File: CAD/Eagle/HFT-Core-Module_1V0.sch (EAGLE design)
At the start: 372 parts, among them Q0521 ABS07-32.768KHZ, Q0811 ABM03B-32.000MHZ, Q0911 ABM3B-16MHZ-10-R50-1-U, T1201 MMBT2222, T1202 MMBT2222, T1203 MMBT2222, U0111 STM32L4Z_144PIN_SMPS, U0431 PAM2305AAB120, U0601 LM4120IM5-3.0, U0611 MAX5217, U0631 CFPT-141-20MHZ, U0641 OPA354, U0701 Si5338, U0801 SX1276, U0901 AX5243, U1011 MAX5136AGTG+, U1101 MCP3911A0-E-SS, U1121 OPA354, U1131 OPA354, U1141 OPA354, U1201 NHD-C0220BIZ_2X20CHARS, U1301 MPU-9250, U1311 MS5607-02BA03, U1321 SHT31-DIS, U1401 SOLARPANEL_3V3_5MA1_25MM_X_20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, U1402 SPV1040T, U1501 TS5A23166, U1601 PAM2305AAB330, U1701 TS5A23166, U1801 TS5A23166, U1901 TS5A23166, X1261 TTE_EN11-HSM, X2101 SMA_SMT_AMPHENOL-901-143, X2111 SMA_SMT_AMPHENOL-901-143, X2201 CUI SJ1-3535NS, X2211 CUI SJ1-3535NS, X2311 2X20/90_1MM27_HARWIN_M50-3202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, X2312 2X20/90_1MM27_HARWIN_M50-3202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, X2321 2X20/90_1MM27_HARWIN_M50-3202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, X2322 2X20/90_1MM27_HARWIN_M50-3202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, X2331 2X20/90_1MM27_HARWIN_M50-3202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, X2332 2X20/90_1MM27_HARWIN_M50-3202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

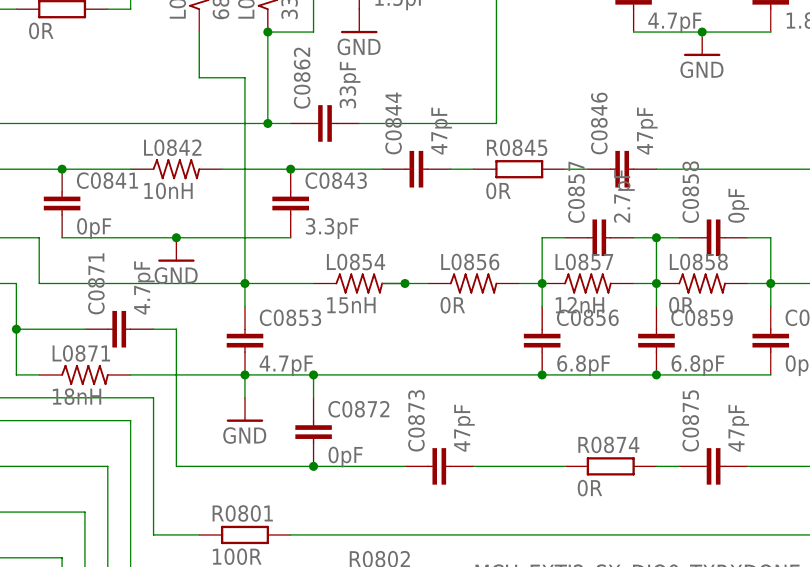
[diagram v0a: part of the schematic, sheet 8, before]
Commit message: HW_1V0_trySX - SX1276 some RF components placed
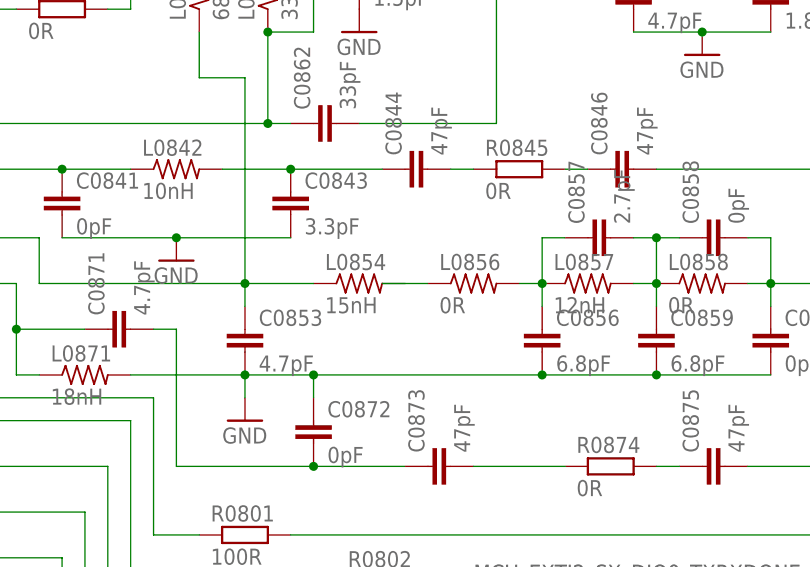
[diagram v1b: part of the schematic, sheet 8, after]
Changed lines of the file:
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@@
 <pinref part="L0854" gate="G$1" pin="2"/>
 <wire x1="172.72" y1="91.44" x2="175.26" y2="91.44" width="0.1524" layer="91"/>
-<junction x="172.72" y="91.44"/>
 </segment>
 </net>

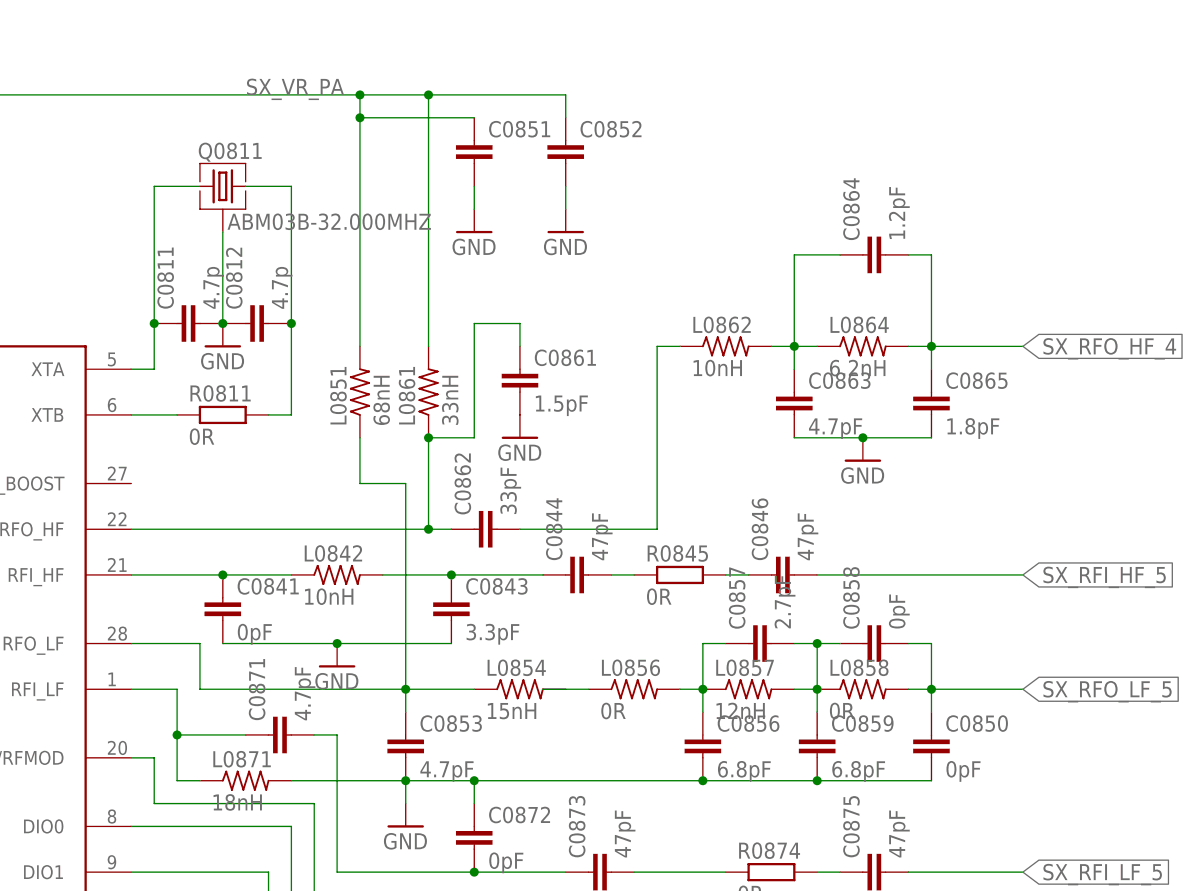
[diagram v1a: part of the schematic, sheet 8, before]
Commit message: HW_1V0_trySX - SX1276 RF components are placed
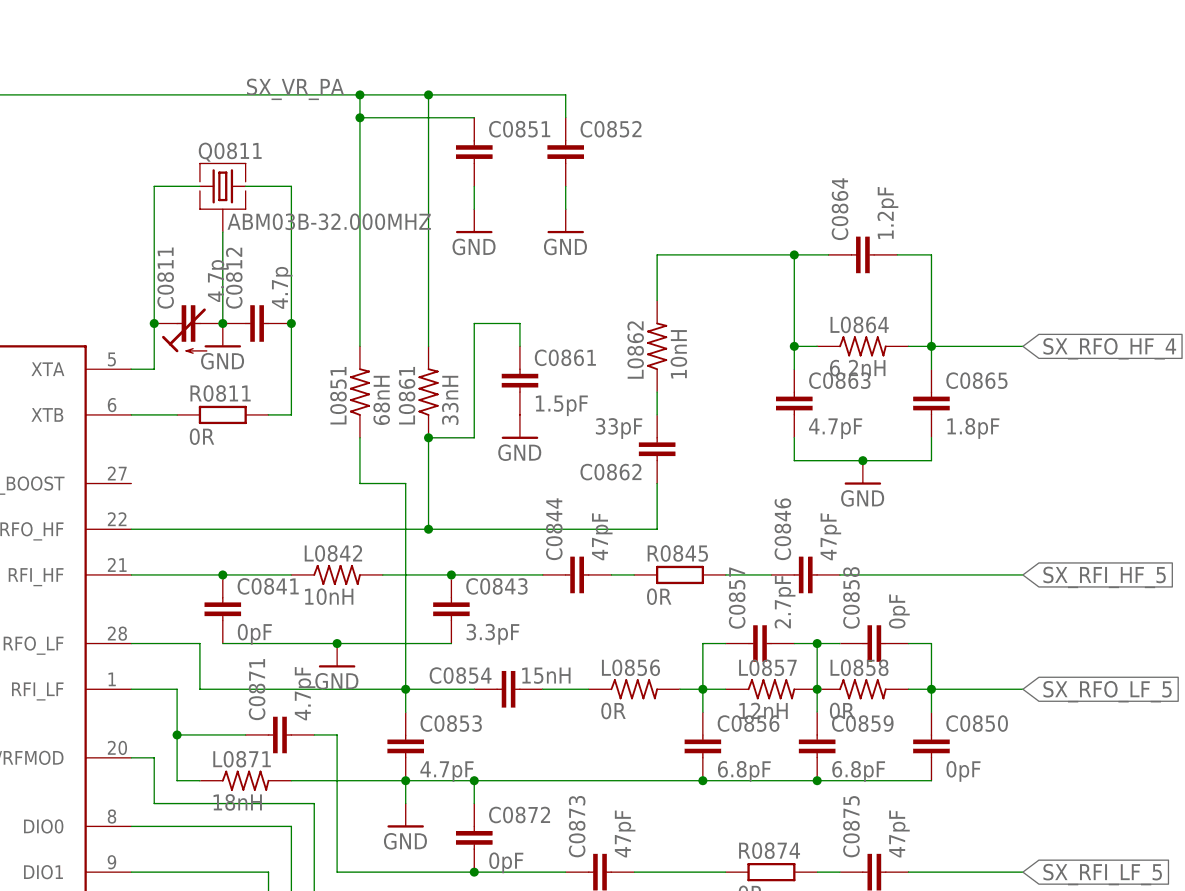
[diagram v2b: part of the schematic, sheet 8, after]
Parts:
- removed L0854: 15nH, rcl:R-US_R0603
- added C0854: 15nH, rcl:C-EUC0603
- C0811: device rcl:C-EUC0603 -> df4iah_c-trimm:C-TRIMM3MM2_2MM5
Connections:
- net GND: now also C0811.A; no longer C0811.2
- net SX_RFO_LF: now also C0854.1; no longer L0854.1
- net SX_RFO_LF_2: now also C0854.2; no longer L0854.2
- net SX_XTA: now also C0811.E; no longer C0811.1
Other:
- moved on the sheet: C0846, C0862, C0864, L0857, L0862
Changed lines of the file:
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@@
 <part name="R0811" library="rcl" deviceset="R-EU_" device="R0603" value="0R"/>
 <part name="GND0811" library="df4iah_supply" deviceset="GND" device=""/>
-<part name="C0811" library="rcl" deviceset="C-EU" device="C0603" value="4.7p"/>
+<part name="C0811" library="df4iah_c-trimm" deviceset="C-TRIMM" device="3MM2_2MM5" value="4.7p"/>
 <part name="C0812" library="rcl" deviceset="C-EU" device="C0603" value="4.7p"/>
 <part name="C0806" library="rcl" deviceset="C-EU" device="C0603" value="100n"/>
@@
 <part name="R0874" library="rcl" deviceset="R-EU_" device="R0603" value="0R"/>
 <part name="C0871" library="rcl" deviceset="C-EU" device="C0603" value="4.7pF"/>
-<part name="L0854" library="rcl" deviceset="R-US_" device="R0603" value="15nH"/>
+<part name="C0854" library="rcl" deviceset="C-EU" device="C0603" value="15nH"/>
 <part name="R0801" library="rcl" deviceset="R-EU_" device="R0603" value="100R"/>
 <part name="R0803" library="rcl" deviceset="R-EU_" device="R0603" value="47R"/>
@@
 <instance part="C0844" gate="G$1" x="172.72" y="104.14" rot="R90"/>
 <instance part="R0845" gate="G$1" x="185.42" y="104.14"/>
-<instance part="C0846" gate="G$1" x="195.58" y="104.14" rot="R90"/>
+<instance part="C0846" gate="G$1" x="198.12" y="104.14" rot="R90"/>
 <instance part="L0861" gate="G$1" x="157.48" y="124.46" rot="R90"/>
-<instance part="C0862" gate="G$1" x="162.56" y="109.22" rot="R90"/>
+<instance part="C0862" gate="G$1" x="182.88" y="116.84" rot="R180"/>
 <instance part="C0861" gate="G$1" x="167.64" y="127"/>
 <instance part="GND0861" gate="1" x="167.64" y="119.38"/>
-<instance part="L0862" gate="G$1" x="190.5" y="129.54"/>
+<instance part="L0862" gate="G$1" x="182.88" y="129.54" rot="R90"/>
 <instance part="L0864" gate="G$1" x="205.74" y="129.54"/>
-<instance part="C0864" gate="G$1" x="205.74" y="139.7" rot="R90"/>
+<instance part="C0864" gate="G$1" x="204.47" y="139.7" rot="R90"/>
 <instance part="C0863" gate="G$1" x="198.12" y="124.46"/>
 <instance part="C0865" gate="G$1" x="213.36" y="124.46"/>
-<instance part="GND0862" gate="1" x="205.74" y="116.84"/>
+<instance part="GND0862" gate="1" x="205.74" y="114.3"/>
 <instance part="C0851" gate="G$1" x="162.56" y="152.4"/>
 <instance part="C0852" gate="G$1" x="172.72" y="152.4"/>
@@
 <instance part="GND0853" gate="1" x="154.94" y="76.2"/>
 <instance part="L0856" gate="G$1" x="180.34" y="91.44"/>
-<instance part="L0857" gate="G$1" x="193.04" y="91.44"/>
+<instance part="L0857" gate="G$1" x="195.58" y="91.44"/>
 <instance part="L0858" gate="G$1" x="205.74" y="91.44"/>
 <instance part="C0856" gate="G$1" x="187.96" y="86.36"/>
@@
 <instance part="R0874" gate="G$1" x="195.58" y="71.12"/>
 <instance part="C0871" gate="G$1" x="139.7" y="86.36" rot="R90"/>
-<instance part="L0854" gate="G$1" x="167.64" y="91.44"/>
+<instance part="C0854" gate="G$1" x="165.1" y="91.44" smashed="yes" rot="R90">
+<attribute name="NAME" x="157.48" y="92.075" size="1.778" layer="95"/>
+<attribute name="VALUE" x="167.64" y="92.075" size="1.778" layer="96"/>
+</instance>
 <instance part="R0801" gate="G$1" x="154.94" y="63.5"/>
 <instance part="R0803" gate="G$1" x="154.94" y="53.34"/>
@@
 <pinref part="Q0811" gate="G$1" pin="3"/>
 <wire x1="134.62" y1="132.08" x2="134.62" y2="142.24" width="0.1524" layer="91"/>
-<pinref part="C0811" gate="G$1" pin="2"/>
+<pinref part="C0811" gate="G$1" pin="A"/>
 <junction x="134.62" y="132.08"/>
 <pinref part="C0812" gate="G$1" pin="1"/>
@@
 <pinref part="C0863" gate="G$1" pin="2"/>
 <pinref part="C0865" gate="G$1" pin="2"/>
-<wire x1="198.12" y1="119.38" x2="205.74" y2="119.38" width="0.1524" layer="91"/>
+<wire x1="198.12" y1="119.38" x2="198.12" y2="116.84" width="0.1524" layer="91"/>
+<wire x1="198.12" y1="116.84" x2="205.74" y2="116.84" width="0.1524" layer="91"/>
 <pinref part="GND0862" gate="1" pin="GND"/>
-<wire x1="205.74" y1="119.38" x2="213.36" y2="119.38" width="0.1524" layer="91"/>
-<junction x="205.74" y="119.38"/>
+<wire x1="205.74" y1="116.84" x2="213.36" y2="116.84" width="0.1524" layer="91"/>
+<wire x1="213.36" y1="116.84" x2="213.36" y2="119.38" width="0.1524" layer="91"/>
+<junction x="205.74" y="116.84"/>
 </segment>
 <segment>
@@
 <wire x1="127" y1="132.08" x2="127" y2="147.32" width="0.1524" layer="91"/>
 <wire x1="127" y1="147.32" x2="132.08" y2="147.32" width="0.1524" layer="91"/>
-<pinref part="C0811" gate="G$1" pin="1"/>
+<pinref part="C0811" gate="G$1" pin="E"/>
 <junction x="127" y="132.08"/>
 </segment>
@@
 <pinref part="R0845" gate="G$1" pin="2"/>
 <pinref part="C0846" gate="G$1" pin="1"/>
-<wire x1="190.5" y1="104.14" x2="193.04" y2="104.14" width="0.1524" layer="91"/>
+<wire x1="190.5" y1="104.14" x2="195.58" y2="104.14" width="0.1524" layer="91"/>
 </segment>
 </net>
@@
 <wire x1="124.46" y1="109.22" x2="157.48" y2="109.22" width="0.1524" layer="91"/>
 <wire x1="157.48" y1="109.22" x2="157.48" y2="119.38" width="0.1524" layer="91"/>
-<wire x1="157.48" y1="109.22" x2="160.02" y2="109.22" width="0.1524" layer="91"/>
+<wire x1="157.48" y1="109.22" x2="182.88" y2="109.22" width="0.1524" layer="91"/>
+<wire x1="182.88" y1="109.22" x2="182.88" y2="114.3" width="0.1524" layer="91"/>
 <junction x="157.48" y="109.22"/>
 <pinref part="C0862" gate="G$1" pin="1"/>
@@
 <segment>
 <pinref part="C0862" gate="G$1" pin="2"/>
-<wire x1="167.64" y1="109.22" x2="182.88" y2="109.22" width="0.1524" layer="91"/>
-<wire x1="182.88" y1="109.22" x2="182.88" y2="129.54" width="0.1524" layer="91"/>
+<wire x1="182.88" y1="121.92" x2="182.88" y2="124.46" width="0.1524" layer="91"/>
 <pinref part="L0862" gate="G$1" pin="1"/>
-<wire x1="182.88" y1="129.54" x2="185.42" y2="129.54" width="0.1524" layer="91"/>
 </segment>
 </net>
 <net name="SX_RFO_HF_3" class="0">
 <segment>
-<pinref part="L0864" gate="G$1" pin="1"/>
 <pinref part="L0862" gate="G$1" pin="2"/>
-<wire x1="200.66" y1="129.54" x2="198.12" y2="129.54" width="0.1524" layer="91"/>
 <pinref part="C0863" gate="G$1" pin="1"/>
-<wire x1="198.12" y1="129.54" x2="195.58" y2="129.54" width="0.1524" layer="91"/>
+<wire x1="198.12" y1="139.7" x2="182.88" y2="139.7" width="0.1524" layer="91"/>
+<wire x1="182.88" y1="139.7" x2="182.88" y2="134.62" width="0.1524" layer="91"/>
+<wire x1="198.12" y1="139.7" x2="198.12" y2="129.54" width="0.1524" layer="91"/>
+<junction x="198.12" y="139.7"/>
+<pinref part="C0864" gate="G$1" pin="1"/>
 <wire x1="198.12" y1="129.54" x2="198.12" y2="127" width="0.1524" layer="91"/>
+<wire x1="198.12" y1="139.7" x2="201.93" y2="139.7" width="0.1524" layer="91"/>
+<pinref part="L0864" gate="G$1" pin="1"/>
+<wire x1="198.12" y1="129.54" x2="200.66" y2="129.54" width="0.1524" layer="91"/>
 <junction x="198.12" y="129.54"/>
-<pinref part="C0864" gate="G$1" pin="1"/>
-<wire x1="198.12" y1="129.54" x2="198.12" y2="139.7" width="0.1524" layer="91"/>
-<wire x1="198.12" y1="139.7" x2="203.2" y2="139.7" width="0.1524" layer="91"/>
 </segment>
 </net>
@@
 <junction x="213.36" y="129.54"/>
 <pinref part="C0864" gate="G$1" pin="2"/>
-<wire x1="210.82" y1="139.7" x2="213.36" y2="139.7" width="0.1524" layer="91"/>
+<wire x1="209.55" y1="139.7" x2="213.36" y2="139.7" width="0.1524" layer="91"/>
 <wire x1="213.36" y1="139.7" x2="213.36" y2="129.54" width="0.1524" layer="91"/>
 <wire x1="213.36" y1="129.54" x2="223.52" y2="129.54" width="0.1524" layer="91"/>
@@
 <segment>
 <pinref part="C0846" gate="G$1" pin="2"/>
-<wire x1="200.66" y1="104.14" x2="223.52" y2="104.14" width="0.1524" layer="91"/>
+<wire x1="203.2" y1="104.14" x2="223.52" y2="104.14" width="0.1524" layer="91"/>
 <label x="223.52" y="104.14" size="1.778" layer="95" xref="yes"/>
 </segment>
@@
 <pinref part="C0853" gate="G$1" pin="1"/>
 <wire x1="154.94" y1="91.44" x2="154.94" y2="88.9" width="0.1524" layer="91"/>
-<pinref part="L0854" gate="G$1" pin="1"/>
+<pinref part="C0854" gate="G$1" pin="1"/>
 </segment>
 </net>
 <net name="SX_RFO_LF_2" class="0">
 <segment>
-<wire x1="170.18" y1="91.44" x2="172.72" y2="91.44" width="0.1524" layer="91"/>
 <pinref part="L0856" gate="G$1" pin="1"/>
-<pinref part="L0854" gate="G$1" pin="2"/>
-<wire x1="172.72" y1="91.44" x2="175.26" y2="91.44" width="0.1524" layer="91"/>
+<pinref part="C0854" gate="G$1" pin="2"/>
+<wire x1="170.18" y1="91.44" x2="175.26" y2="91.44" width="0.1524" layer="91"/>
 </segment>
 </net>
@@
 <pinref part="C0856" gate="G$1" pin="1"/>
 <wire x1="187.96" y1="91.44" x2="187.96" y2="88.9" width="0.1524" layer="91"/>
-<junction x="187.96" y="91.44"/>
+<wire x1="190.5" y1="91.44" x2="187.96" y2="91.44" width="0.1524" layer="91"/>
 <wire x1="187.96" y1="91.44" x2="187.96" y2="96.52" width="0.1524" layer="91"/>
 <pinref part="C0857" gate="G$1" pin="1"/>
 <wire x1="187.96" y1="96.52" x2="190.5" y2="96.52" width="0.1524" layer="91"/>
+<junction x="187.96" y="91.44"/>
 </segment>
 </net>
@@
 <pinref part="L0857" gate="G$1" pin="2"/>
 <pinref part="L0858" gate="G$1" pin="1"/>
-<wire x1="198.12" y1="91.44" x2="200.66" y2="91.44" width="0.1524" layer="91"/>
 <pinref part="C0859" gate="G$1" pin="1"/>
 <wire x1="200.66" y1="91.44" x2="200.66" y2="88.9" width="0.1524" layer="91"/>

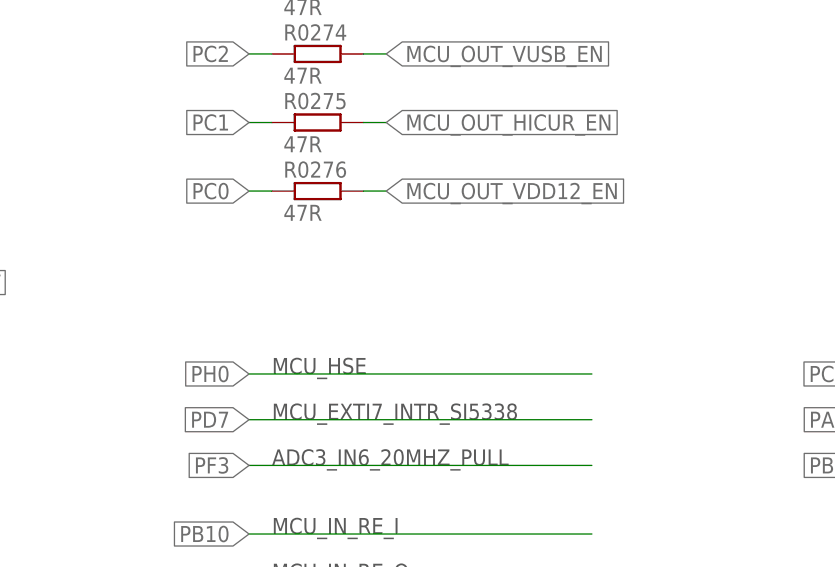
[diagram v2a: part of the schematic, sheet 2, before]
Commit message: HW_1V0_trySX - SX1276 - 3x PE4259 RF switches placed
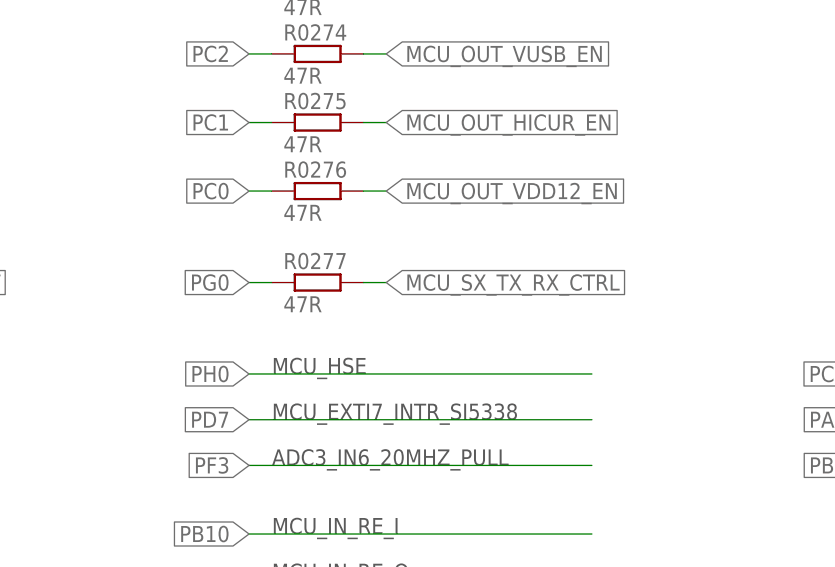
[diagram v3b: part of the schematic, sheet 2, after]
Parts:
- added C0911, C0921, C0991, C0992, C0993, C0994, C0996, C0999: (no value), rcl:C-EUC0603
- added L0995: 10nH, rcl:R-US_R0603
- added R0277: 47R, rcl:R-EU_R0603
- added U0911, U0921, U0991: PE4259, df4iah_rf:PE4259
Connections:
- new net MCU_SX_TX_RX_CTRL: R0277.2, U0991.CTRL
- new net SX_ANT_1: C0993.1, U0991.RFC
- new net SX_ANT_2: C0993.2, C0994.1, L0995.1
- new net SX_HF_1: C0991.1, U0911.RFC
- new net SX_HF_2: C0991.2, U0991.RF1
- new net SX_LF_1: C0992.1, U0921.RFC
- new net SX_LF_2: C0992.2, U0991.RF2
- net +3V3: now also C0911.1, C0921.1, C0999.1, U0911.VDD_!CTRL, U0921.VDD_!CTRL, U0991.VDD_!CTRL
- net CH1_ANT: now also C0996.1, L0995.2
- net GND: now also C0911.2, C0921.2, C0994.2, C0996.2, C0999.2, U0911.GND, U0921.GND, U0991.GND
- net PG0: now also R0277.1
- net SX_RFI_HF_5: now also U0911.RF2
- net SX_RFI_LF_5: now also U0921.RF2
- net SX_RFO_HF_4: now also U0911.RF1
- net SX_RFO_LF_5: now also U0921.RF1
- net SX_RXTX_2: now also U0911.CTRL, U0921.CTRL
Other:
- note added: "HF: high / LF: low"
